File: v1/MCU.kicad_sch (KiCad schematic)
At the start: 12 parts, among them U6 ESP32-WROOM-E, U7 CH340N, Y1 32.768khz

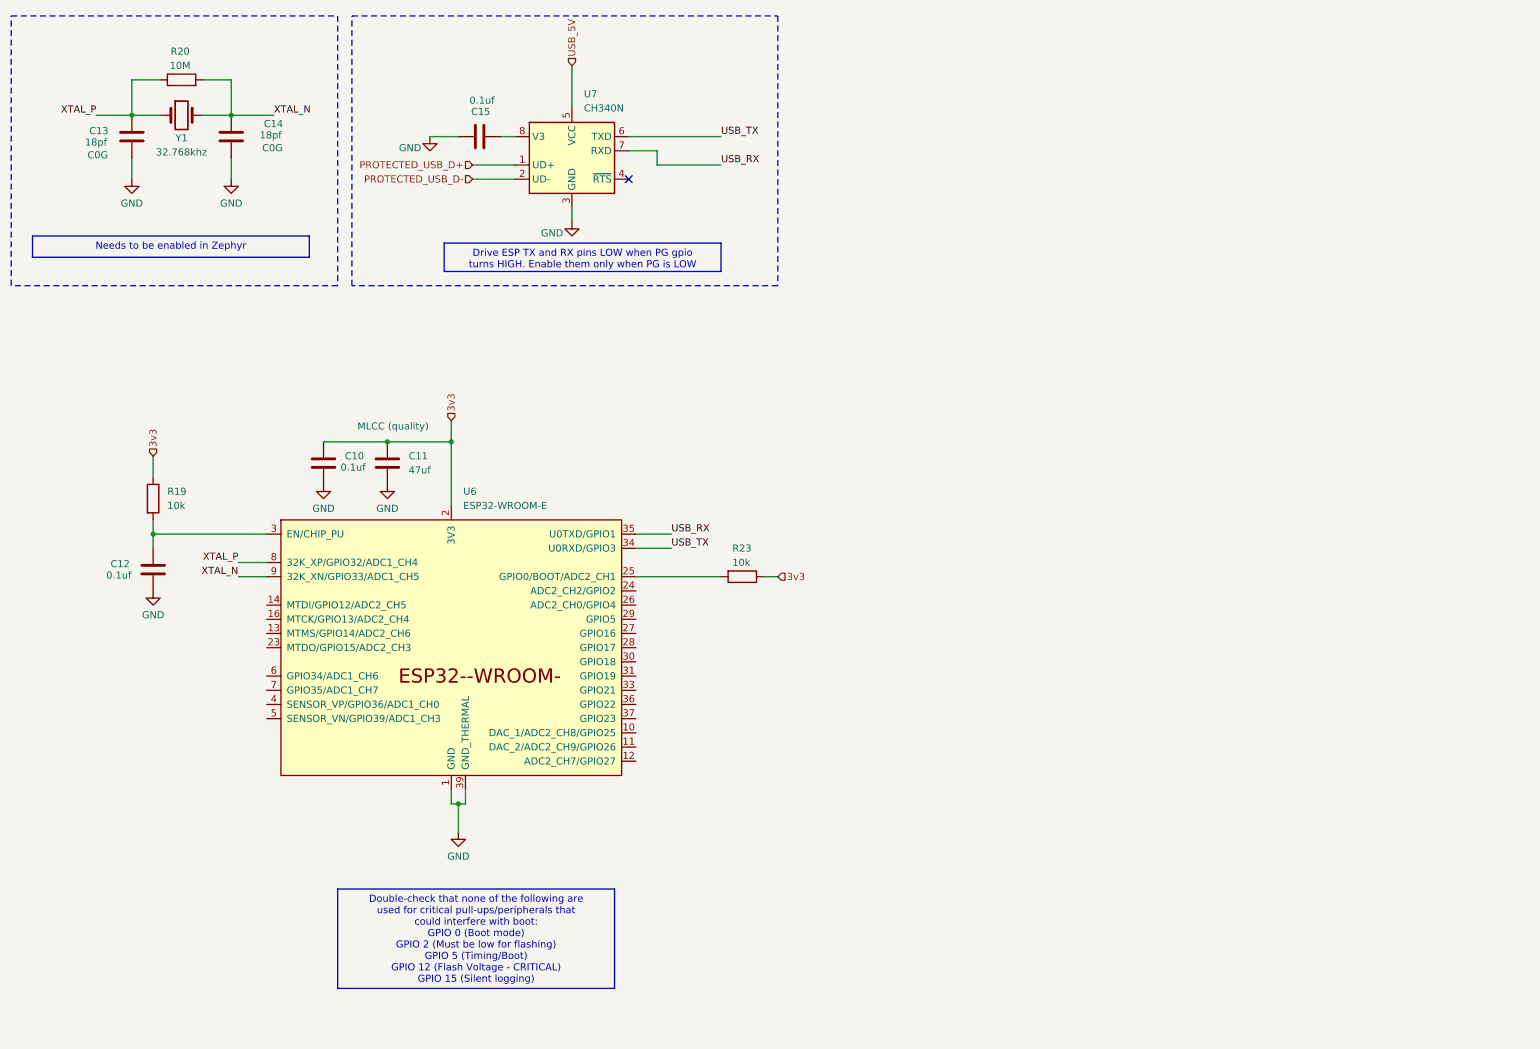
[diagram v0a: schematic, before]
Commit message: Updated layout
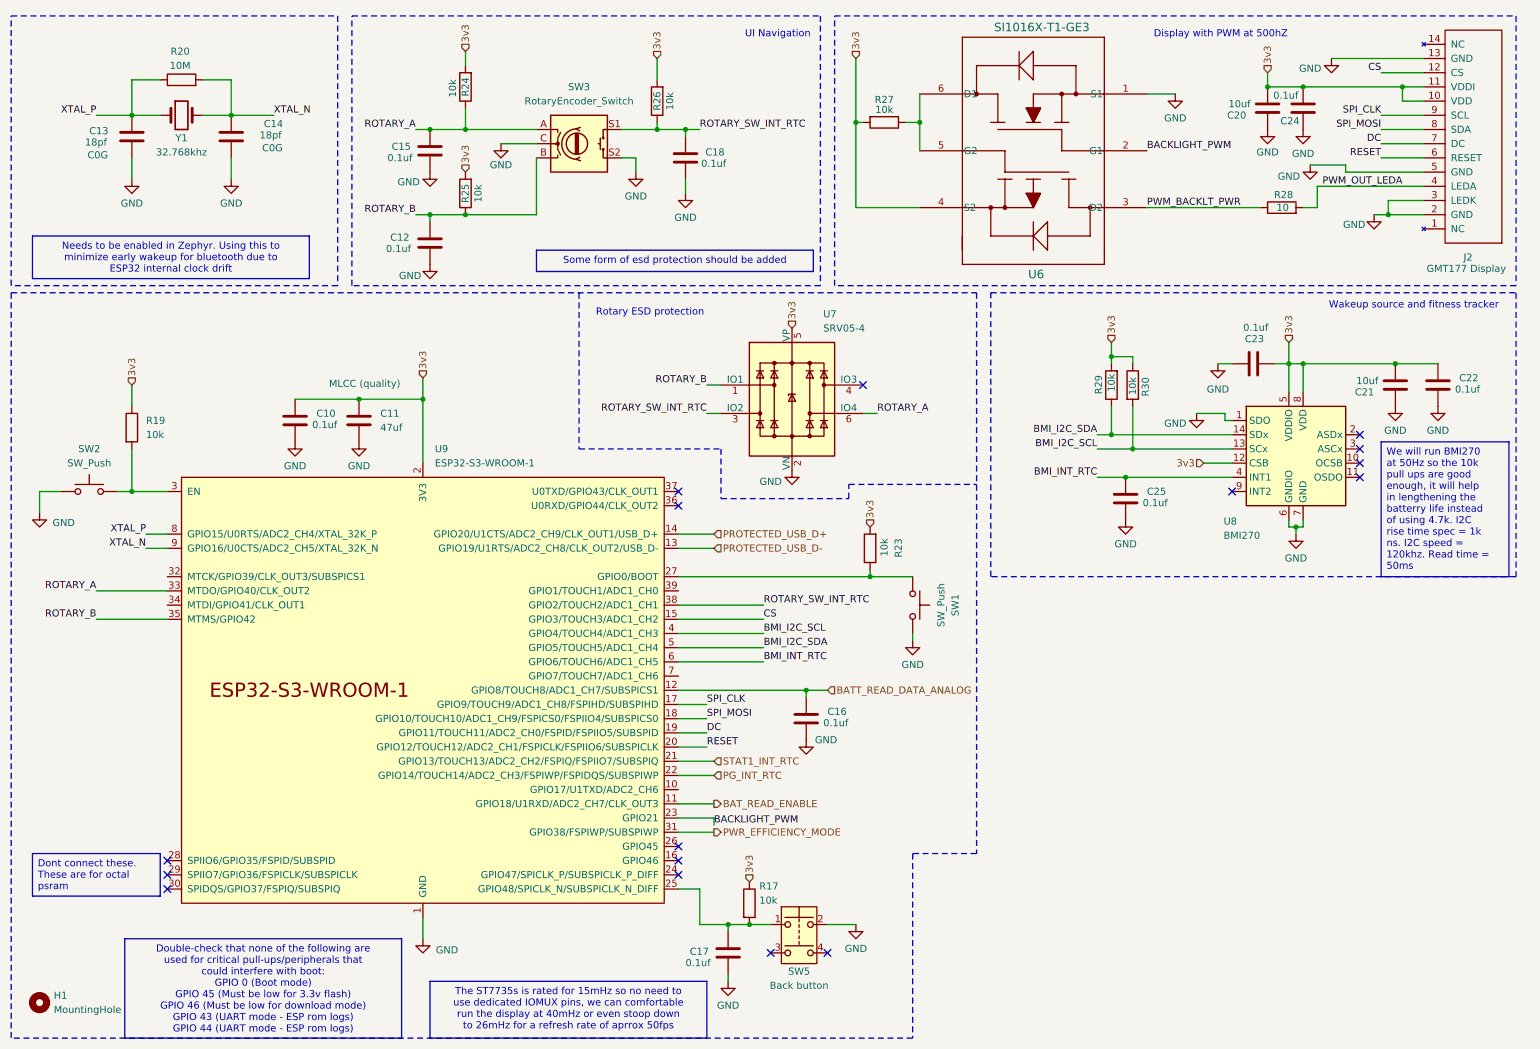
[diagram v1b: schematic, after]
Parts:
- removed U6: ESP32-WROOM-E, PCM_Espressif:ESP32-WROOM-32E, symbol PCM_Espressif:ESP32-WROOM-E
- removed U7: CH340N, Package_SO:SOP-8_3.9x4.9mm_P1.27mm, symbol Interface_USB:CH340N
- added C16, C17, C18, C22, C23, C24, C25: 0.1uf, Capacitor_SMD:C_0603_1608Metric_Pad1.08x0.95mm_HandSolder, symbol Device:C
- added C20, C21: 10uf, Capacitor_SMD:C_0603_1608Metric_Pad1.08x0.95mm_HandSolder, symbol Device:C
- added H1: MountingHole, MountingHole:MountingHole_3.2mm_M3_ISO14580, symbol Mechanical:MountingHole
- added J2: GMT177 Display, Connector_FFC-FPC:TE_1-1734839-3_1x13-1MP_P0.5mm_Horizontal, symbol Connector:Conn_01x14_Pin
- added R17, R24, R25, R26, R27, R29, R30: 10k, Resistor_SMD:R_0603_1608Metric_Pad0.98x0.95mm_HandSolder, symbol Device:R
- added R28: 10, Resistor_SMD:R_0603_1608Metric_Pad0.98x0.95mm_HandSolder, symbol Device:R
- added SW1, SW2: SW_Push, Button_Switch_SMD:SW_SPST_B3U-1000P, symbol Switch:SW_Push
- added SW3: RotaryEncoder_Switch, Rotary_Encoder:RotaryEncoder_Bourns_Horizontal_PEC12R-2x17F-Sxxxx, symbol Device:RotaryEncoder_Switch
- added SW5: Back button, Right angle switch:EVQPUC02K, symbol Switch:SW_Push_Dual
- added U6: SI1016X-T1-GE3, footprints:SOT_X-T1-GE3_VIS-M, symbol Si1016X:SI1016X-T1-GE3
- added U7: SRV05-4, Package_TO_SOT_SMD:SOT-23-6, symbol Power_Protection:SRV05-4
- added U8: BMI270, Package_LGA:Bosch_LGA-14_3x2.5mm_P0.5mm, symbol Sensor_Motion:BMI160
- added U9: ESP32-S3-WROOM-1, PCM_Espressif:ESP32-S3-WROOM-1, symbol PCM_Espressif:ESP32-S3-WROOM-1
- C11: footprint Capacitor_SMD:C_0603_1608Metric_Pad1.08x0.95mm_HandSolder -> Capacitor_SMD:C_1210_3225Metric_Pad1.33x2.70mm_HandSolder
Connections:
- net 3v3: now also R23.2, C20.2, C21.2, C22.1, C23.2, C24.1, J2.10 (VDD), J2.11 (VDDI), R17.1, R24.2, R25.2, R26.2, R27.2, R29.2, R30.1, U6.4 (S2), U7.5 (VP), U8.12 (CSB), U8.5 (VDDIO), U8.8 (VDD), U9.2 (3V3); no longer R23.1
- net GND: now also C15.2, C16.2, C17.2, C18.2, C20.1, C21.1, C22.2, C23.1, C24.2, C25.2, J2.13 (GND), J2.2 (GND), J2.3 (LEDK), J2.5 (GND), SW1.2, SW2.1, SW3.C, SW3.S2, SW5.2, U6.1 (S1), U7.2 (VN), U8.1 (SDO), U8.6 (GNDIO), U8.7 (GND), U9.1 (GND), U9.40 (GND), U9.41 (GND); no longer C15.1
- net PROTECTED_USB_D+: now also U9.14 (GPIO20/U1CTS/ADC2_CH9/CLK_OUT1/USB_D+)
- net PROTECTED_USB_D-: now also U9.13 (GPIO19/U1RTS/ADC2_CH8/CLK_OUT2/USB_D-)
- net XTAL_N: now also U9.9 (GPIO16/U0CTS/ADC2_CH5/XTAL_32K_N)
- net XTAL_P: now also U9.8 (GPIO15/U0RTS/ADC2_CH4/XTAL_32K_P)
- net at R19.2: now also SW2.2, U9.3 (EN); no longer C12.1
- new net: C17.1, R17.2, SW5.1, U9.25 (GPIO48/SPICLK_N/SUBSPICLK_N_DIFF)
- new net: R27.1, U6.5 (G2), U6.6 (D1)
- new net: R23.1, SW1.1, U9.27 (GPIO0/BOOT)
- new net BACKLIGHT_PWM: U6.2 (G1), U9.23 (GPIO21)
- new net BATT_READ_DATA_ANALOG: C16.1, U9.12 (GPIO8/TOUCH8/ADC1_CH7/SUBSPICS1)
- new net BAT_READ_ENABLE: U9.11 (GPIO18/U1RXD/ADC2_CH7/CLK_OUT3)
- new net BMI_I2C_SCL: R30.2, U8.13 (SCx), U9.4 (GPIO4/TOUCH4/ADC1_CH3)
- new net BMI_I2C_SDA: R29.1, U8.14 (SDx), U9.5 (GPIO5/TOUCH5/ADC1_CH4)
- new net BMI_INT_RTC: C25.1, U8.4 (INT1), U9.6 (GPIO6/TOUCH6/ADC1_CH5)
- new net CS: J2.12 (CS), U9.15 (GPIO3/TOUCH3/ADC1_CH2)
- new net DC: J2.7 (DC), U9.19 (GPIO11/TOUCH11/ADC2_CH0/FSPID/FSPIIO5/SUBSPID)
- new net PG_INT_RTC: U9.22 (GPIO14/TOUCH14/ADC2_CH3/FSPIWP/FSPIDQS/SUBSPIWP)
- new net PWM_BACKLT_PWR: R28.1, U6.3 (D2)
- new net PWM_OUT_LEDA: J2.4 (LEDA), R28.2
- new net PWR_EFFICIENCY_MODE: U9.31 (GPIO38/FSPIWP/SUBSPIWP)
- new net RESET: J2.6 (RESET), U9.20 (GPIO12/TOUCH12/ADC2_CH1/FSPICLK/FSPIIO6/SUBSPICLK)
- new net ROTARY_A: C15.1, R24.1, SW3.A, U7.6 (IO4), U9.33 (MTDO/GPIO40/CLK_OUT2)
- new net ROTARY_B: C12.1, R25.1, SW3.B, U7.1 (IO1), U9.35 (MTMS/GPIO42)
- new net ROTARY_SW_INT_RTC: C18.1, R26.1, SW3.S1, U7.3 (IO2), U9.38 (GPIO2/TOUCH2/ADC1_CH1)
- new net SPI_CLK: J2.9 (SCL), U9.17 (GPIO9/TOUCH9/ADC1_CH8/FSPIHD/SUBSPIHD)
- new net SPI_MOSI: J2.8 (SDA), U9.18 (GPIO10/TOUCH10/ADC1_CH9/FSPICS0/FSPIIO4/SUBSPICS0)
- new net STAT1_INT_RTC: U9.21 (GPIO13/TOUCH13/ADC2_CH2/FSPIQ/FSPIIO7/SUBSPIQ)
- no-connect marks 1 -> 16
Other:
- note added: "Display with PWM at 500hZ"
- note added: "Rotary ESD protection"
- note added: "UI Navigation"
- note added: "Wakeup source and fitness tracker"
- moved on the sheet: C10, C11, R19, R23
